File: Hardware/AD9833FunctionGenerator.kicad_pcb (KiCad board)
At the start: 2 copper layers, 90.7 x 167.6 mm, 55 parts, among them U1 LM7805_TO220

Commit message: Final REVA
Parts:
- added CPWRBP1: 100nF, Capacitor_SMD:C_0805_2012Metric_Pad1.15x1.40mm_HandSolder, B.Cu at (76.2, 116.8)
- added CPWRBP2: 100nF, Capacitor_SMD:C_0805_2012Metric_Pad1.15x1.40mm_HandSolder, B.Cu at (76.2, 123.2)
- moved J_OLEDCONNECTOR1 8.98 mm to (65.7, 69.3)
- moved J_AUX2MAIN2 8.98 mm to (82.1, 81.4)
- moved REF** 8.98 mm to (85.8, 106.9)
- moved REF** 8.98 mm to (52.8, 106.9)
- moved REF** 8.98 mm to (52.8, 67.5)
- moved REF** 8.98 mm to (85.8, 67.5)
- moved R_FUNC1 8.98 mm to (57.2, 93.9)
- moved R_MODE1 8.98 mm to (63.3, 93.9)
- moved R_RANGE1 8.98 mm to (83.3, 93.9)
- moved SW_MODE1 8.98 mm to (66.1, 98.5)
- moved SW_RANGE1 8.98 mm to (78.6, 98.5)
- moved SW_FUNC1 8.98 mm to (53.4, 98.5)
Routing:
- net /+12V: track 322.5 -> 331.0 mm
- net /-12V: track 223.3 -> 231.0 mm
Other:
- board size 90.7 x 167.6 mm -> 81.8 x 167.6 mm
- board text added: "DDS VCO Chris Sutton RevA 20-10-18"

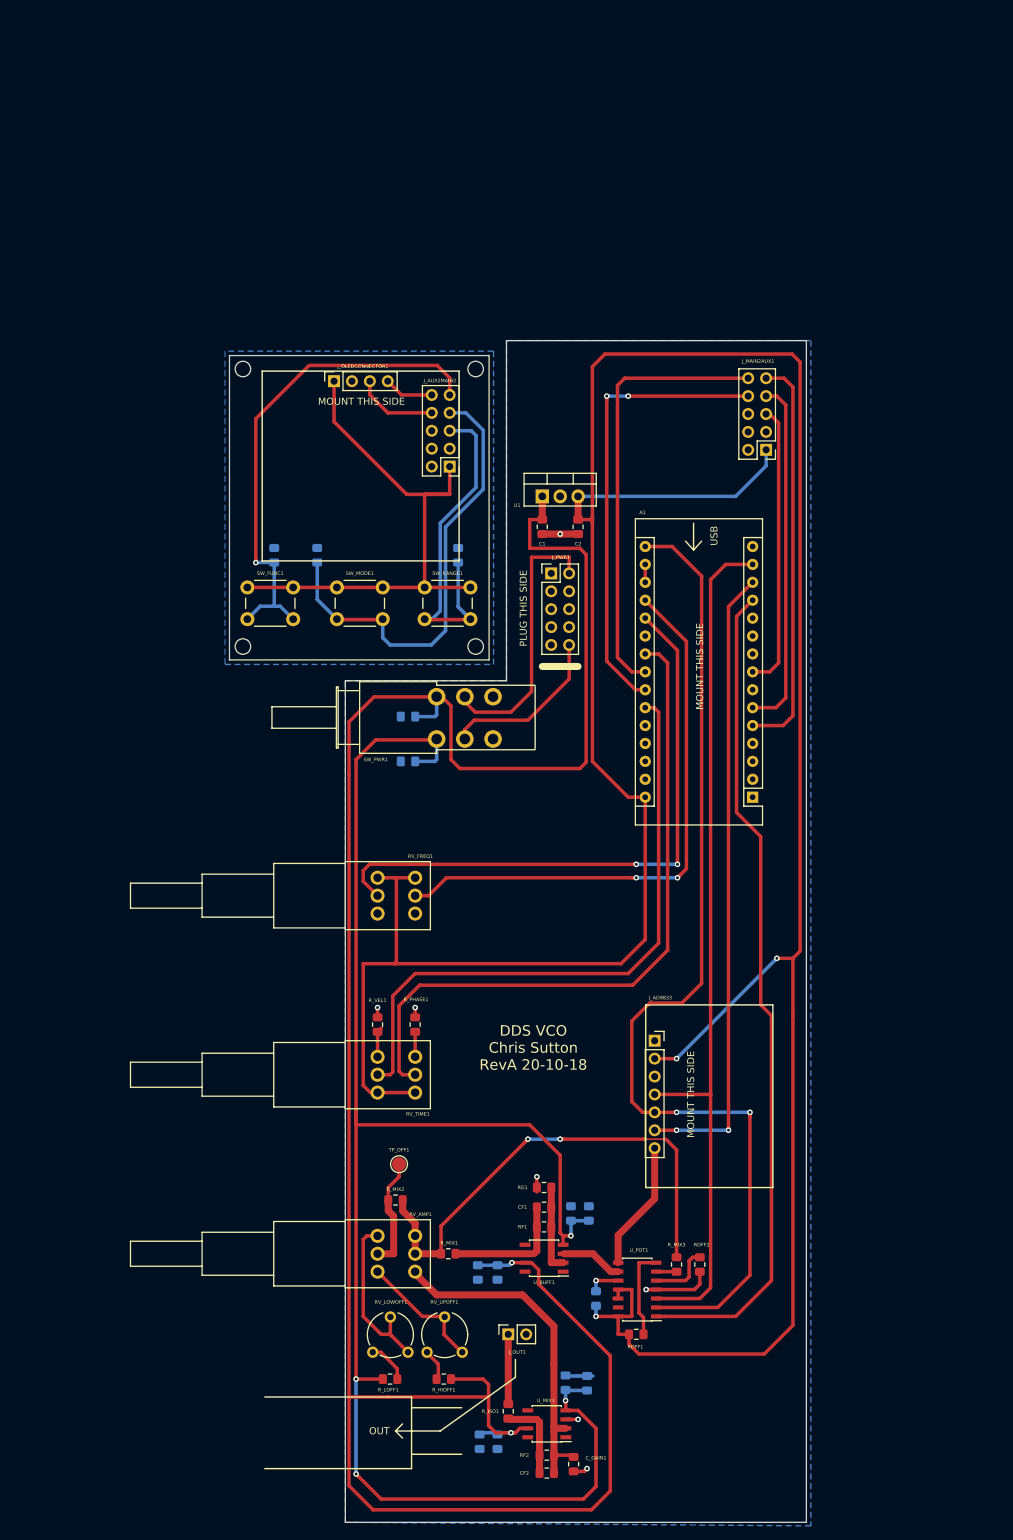
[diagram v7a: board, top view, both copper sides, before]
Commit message: refactored to 4U height
Previous board layout form factor was slightly too large for 4U tolerances
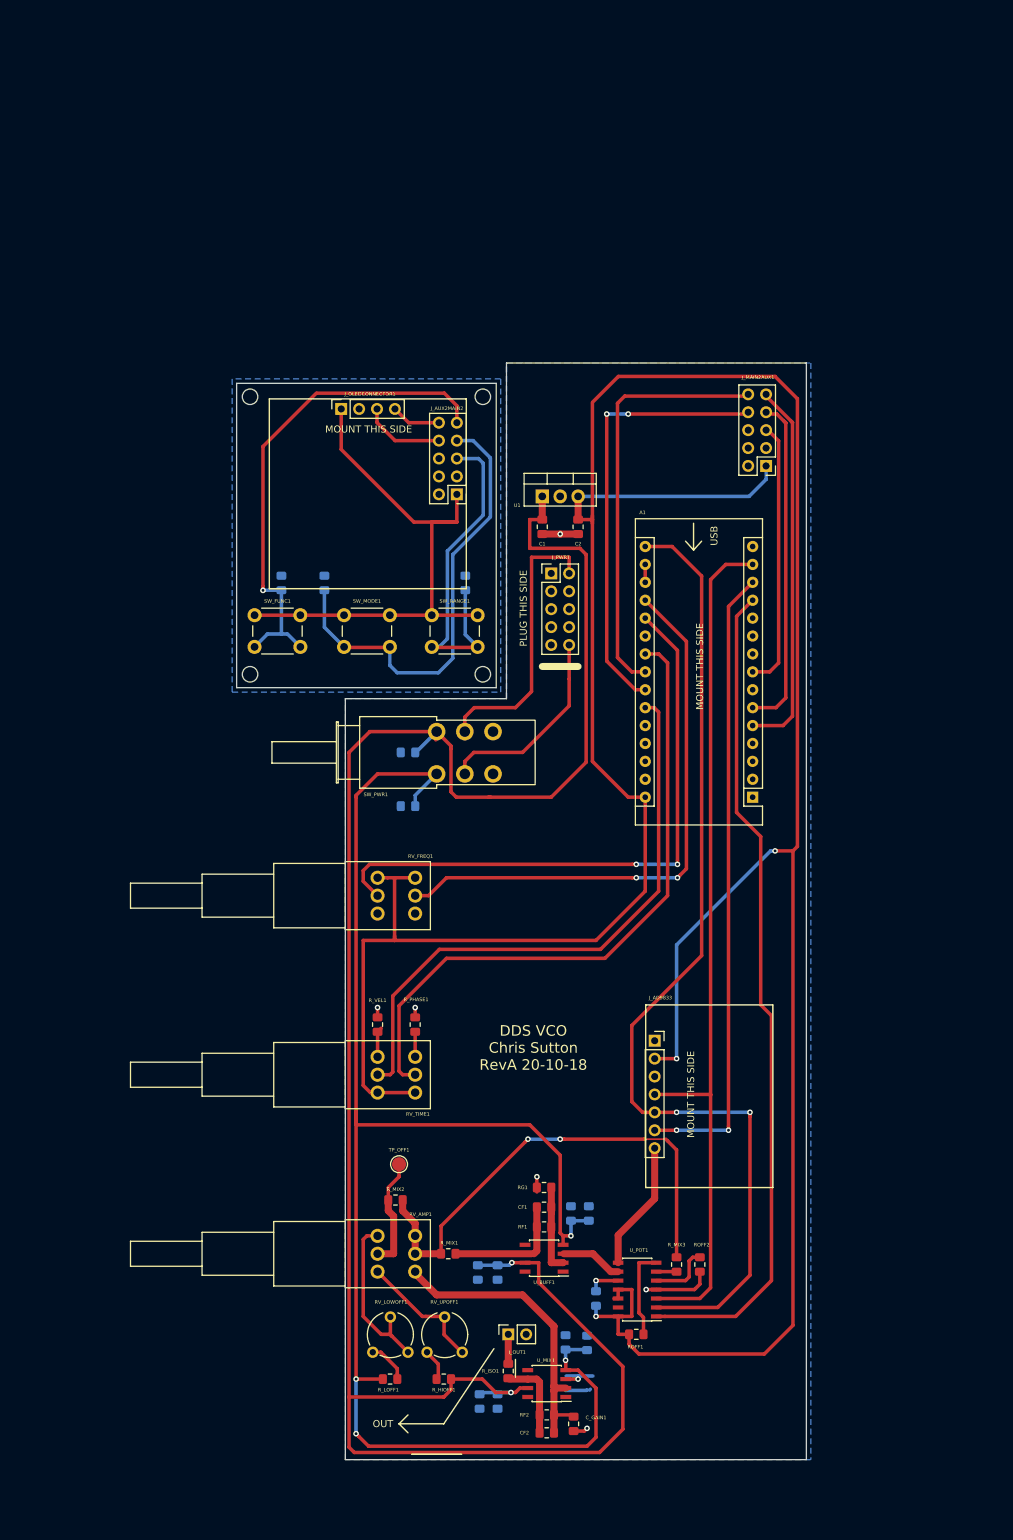
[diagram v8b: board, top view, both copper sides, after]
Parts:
- moved CPWRBP2 6.35 mm to (76.2, 129.5)
- moved CF2 5.72 mm to (95.9, 218.4)
- moved C_GAIN1 5.72 mm to (99.7, 217.2)
- moved C_MIXBP1 5.72 mm to (86.4, 214.0)
- moved C_MIXBP2 5.72 mm to (88.9, 214.0)
- moved C_MIXBP3 5.72 mm to (98.6, 205.6)
- moved C_MIXBP4 5.72 mm to (101.6, 205.7)
- moved RF2 5.72 mm to (95.9, 215.9)
- moved R_ISO1 5.72 mm to (90.4, 209.7)
- moved U_MIX1 5.71 mm to (95.9, 211.5)
- moved CPWRBP1 5.08 mm to (76.2, 121.9)
- moved SW_PWR1 4.95 mm to (80.3, 121.9)
- moved J_OLEDCONNECTOR1 4.07 mm to (66.7, 73.2)
- moved J_AUX2MAIN2 4.07 mm to (83.1, 85.3)
- moved R_RANGE1 4.07 mm to (84.3, 97.9)
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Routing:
- net /+12V: track 331.0 -> 304.9 mm
- net /-12V: track 231.0 -> 217.6 mm
- net Net-(CF2-Pad2): track 48.6 -> 43.0 mm
- net /OutputSection/SIGOUT: track 10.0 -> 4.54 mm
- net Net-(J_PWR1-Pad10): track 23.9 -> 28.5 mm
- net /PHASE1: track 97.6 -> 93.1 mm
- net /VEL1: track 88.9 -> 84.6 mm
- net /WAVEBTN: track 57.2 -> 53.4 mm
- net /GND: track 32.0 -> 35.3 mm
- net Net-(J_PWR1-Pad2): track 38.7 -> 41.8 mm
- net /SCK: track 146.8 -> 144.1 mm
- net /SCL: track 64.8 -> 62.3 mm
- net /SDA: track 62.3 -> 59.8 mm
- net /RANGEBTN: track 40.5 -> 38.0 mm
- net /MODEBTN: track 50.1 -> 47.9 mm
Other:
- board size 81.8 x 167.6 mm -> 80.8 x 155.6 mm
